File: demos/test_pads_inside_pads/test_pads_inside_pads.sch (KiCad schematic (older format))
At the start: 4 parts, among them P1 CONN_1, P2 CONN_1, P3 CONN_1, P4 CONN_1

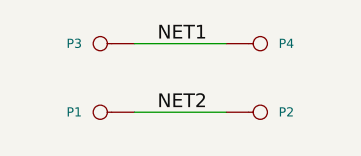
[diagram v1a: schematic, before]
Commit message: polygons in footprint body: fix incorrect calculation of polygons with clearance or outline thickness (fix bug #1511366) Clean demos
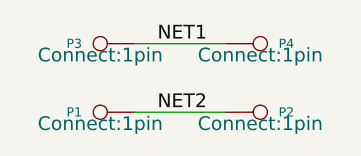
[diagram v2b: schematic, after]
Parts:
- P1, P2, P3, P4: footprint (none) -> Connect:1pin
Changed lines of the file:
@@
-EESchema Schematic File Version 2  date 19/12/2011 12:55:30
+EESchema Schematic File Version 2
 LIBS:power
 LIBS:device
@@
 LIBS:contrib
 LIBS:valves
-EELAYER 25  0
+LIBS:test_pads_inside_pads-cache
+EELAYER 25 0
 EELAYER END
-$Descr A4 11700 8267
+$Descr A4 11693 8268
 encoding utf-8
 Sheet 1 1
@@
 F 0 "P4" H 4380 1450 40  0000 L CNN
 F 1 "CONN_1" H 4300 1505 30  0001 C CNN
+F 2 "Connect:1pin" H 4300 1400 60  0000 C CNN
+F 3 "" H 4300 1450 60  0001 C CNN
 	1    4300 1450
 	1    0    0    -1
@@
 F 0 "P3" H 3680 1450 40  0000 L CNN
 F 1 "CONN_1" H 3600 1505 30  0001 C CNN
+F 2 "Connect:1pin" H 3600 1500 60  0000 C CNN
+F 3 "" H 3600 1450 60  0001 C CNN
 	1    3600 1450
 	-1   0    0    1
@@
 F 0 "P1" H 3680 1750 40  0000 L CNN
 F 1 "CONN_1" H 3600 1805 30  0001 C CNN
+F 2 "Connect:1pin" H 3600 1800 60  0000 C CNN
+F 3 "" H 3600 1750 60  0001 C CNN
 	1    3600 1750
 	-1   0    0    1
@@
 F 0 "P2" H 4380 1750 40  0000 L CNN
 F 1 "CONN_1" H 4300 1805 30  0001 C CNN
+F 2 "Connect:1pin" H 4300 1700 60  0000 C CNN
+F 3 "" H 4300 1750 60  0001 C CNN
 	1    4300 1750
 	1    0    0    -1
